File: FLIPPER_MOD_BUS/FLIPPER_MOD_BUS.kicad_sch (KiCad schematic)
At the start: 13 parts, among them J1 Conn_01x02, J2 Conn_01x10_Socket, J3 Conn_01x08_Socket, U1 SP3485EN

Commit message: UPDATE FLIPPER MODBUS SHIELD
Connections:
- net DE: now also J2.7 (Pin_7); no longer J2.6 (Pin_6)
- net RE: now also J2.8 (Pin_8); no longer J2.7 (Pin_7)
- net TX: now also J2.6 (Pin_6); no longer J2.4 (Pin_4)
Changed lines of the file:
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@@
   (no_connect (at 76.2 99.822))
   (no_connect (at 76.2 102.362))
-  (no_connect (at 45.72 110.236))
   (no_connect (at 76.2 97.282))
   (no_connect (at 76.2 109.982))
   (no_connect (at 45.72 94.996))
+  (no_connect (at 45.72 100.076))
   (wire (pts (xy 32.004 25.908) (xy 32.004 23.622))
     (stroke (width 0) (type default))
@@
     (stroke (width 0) (type default))
   )
+  (wire (pts (xy 44.196 107.696) (xy 45.72 107.696))
+    (stroke (width 0) (type default))
+  )
+  (wire (pts (xy 26.67 39.878) (xy 26.67 30.988))
+    (stroke (width 0) (type default))
+  )
+  (wire (pts (xy 26.67 23.622) (xy 26.67 25.908))
+    (stroke (width 0) (type default))
+  )
+  (wire (pts (xy 37.338 23.622) (xy 37.338 25.908))
+    (stroke (width 0) (type default))
+  )
+  (wire (pts (xy 32.004 23.622) (xy 26.67 23.622))
+    (stroke (width 0) (type default))
+  )
+  (wire (pts (xy 130.556 27.178) (xy 125.476 27.178))
+    (stroke (width 0) (type default))
+  )
+  (wire (pts (xy 36.322 117.856) (xy 36.322 115.316))
+    (stroke (width 0) (type default))
+  )
+  (wire (pts (xy 53.594 32.258) (xy 53.594 30.734))
+    (stroke (width 0) (type default))
+  )
+  (wire (pts (xy 130.556 29.464) (xy 130.556 27.178))
+    (stroke (width 0) (type default))
+  )
+  (wire (pts (xy 125.476 33.274) (xy 125.476 34.544))
+    (stroke (width 0) (type default))
+  )
+  (wire (pts (xy 89.662 30.988) (xy 89.662 28.702))
+    (stroke (width 0) (type default))
+  )
+  (wire (pts (xy 43.434 37.338) (xy 21.336 37.338))
+    (stroke (width 0) (type default))
+  )
+  (wire (pts (xy 119.634 27.178) (xy 125.476 27.178))
+    (stroke (width 0) (type default))
+  )
+  (wire (pts (xy 43.434 44.958) (xy 32.004 44.958))
+    (stroke (width 0) (type default))
+  )
+  (wire (pts (xy 36.322 97.536) (xy 36.322 99.314))
+    (stroke (width 0) (type default))
+  )
+  (wire (pts (xy 89.662 30.988) (xy 94.488 30.988))
+    (stroke (width 0) (type default))
+  )
+  (wire (pts (xy 130.556 32.004) (xy 130.556 34.544))
+    (stroke (width 0) (type default))
+  )
+  (wire (pts (xy 125.476 36.068) (xy 125.476 34.544))
+    (stroke (width 0) (type default))
+  )
+  (wire (pts (xy 44.196 110.236) (xy 45.72 110.236))
+    (stroke (width 0) (type default))
+  )
+  (wire (pts (xy 21.336 23.622) (xy 26.67 23.622))
+    (stroke (width 0) (type default))
+  )
+  (wire (pts (xy 45.72 97.536) (xy 36.322 97.536))
+    (stroke (width 0) (type default))
+  )
+  (wire (pts (xy 130.556 34.544) (xy 125.476 34.544))
+    (stroke (width 0) (type default))
+  )
+  (wire (pts (xy 83.82 40.894) (xy 89.916 40.894))
+    (stroke (width 0) (type default))
+  )
+  (wire (pts (xy 45.72 92.456) (xy 38.862 92.456))
+    (stroke (width 0) (type default))
+  )
   (wire (pts (xy 44.196 105.156) (xy 45.72 105.156))
     (stroke (width 0) (type default))
   )
-  (wire (pts (xy 26.67 39.878) (xy 26.67 30.988))
-    (stroke (width 0) (type default))
-  )
-  (wire (pts (xy 26.67 23.622) (xy 26.67 25.908))
-    (stroke (width 0) (type default))
-  )
-  (wire (pts (xy 37.338 23.622) (xy 37.338 25.908))
-    (stroke (width 0) (type default))
-  )
-  (wire (pts (xy 32.004 23.622) (xy 26.67 23.622))
-    (stroke (width 0) (type default))
-  )
-  (wire (pts (xy 130.556 27.178) (xy 125.476 27.178))
-    (stroke (width 0) (type default))
-  )
-  (wire (pts (xy 36.322 117.856) (xy 36.322 115.316))
-    (stroke (width 0) (type default))
-  )
-  (wire (pts (xy 53.594 32.258) (xy 53.594 30.734))
-    (stroke (width 0) (type default))
-  )
-  (wire (pts (xy 130.556 29.464) (xy 130.556 27.178))
-    (stroke (width 0) (type default))
-  )
-  (wire (pts (xy 125.476 33.274) (xy 125.476 34.544))
-    (stroke (width 0) (type default))
-  )
-  (wire (pts (xy 89.662 30.988) (xy 89.662 28.702))
-    (stroke (width 0) (type default))
-  )
-  (wire (pts (xy 43.434 37.338) (xy 21.336 37.338))
-    (stroke (width 0) (type default))
-  )
-  (wire (pts (xy 119.634 27.178) (xy 125.476 27.178))
-    (stroke (width 0) (type default))
-  )
-  (wire (pts (xy 43.434 44.958) (xy 32.004 44.958))
-    (stroke (width 0) (type default))
-  )
-  (wire (pts (xy 36.322 97.536) (xy 36.322 99.314))
-    (stroke (width 0) (type default))
-  )
-  (wire (pts (xy 89.662 30.988) (xy 94.488 30.988))
-    (stroke (width 0) (type default))
-  )
-  (wire (pts (xy 130.556 32.004) (xy 130.556 34.544))
-    (stroke (width 0) (type default))
-  )
-  (wire (pts (xy 125.476 36.068) (xy 125.476 34.544))
-    (stroke (width 0) (type default))
-  )
-  (wire (pts (xy 44.196 107.696) (xy 45.72 107.696))
-    (stroke (width 0) (type default))
-  )
-  (wire (pts (xy 21.336 23.622) (xy 26.67 23.622))
-    (stroke (width 0) (type default))
-  )
-  (wire (pts (xy 45.72 97.536) (xy 36.322 97.536))
-    (stroke (width 0) (type default))
-  )
-  (wire (pts (xy 130.556 34.544) (xy 125.476 34.544))
-    (stroke (width 0) (type default))
-  )
-  (wire (pts (xy 83.82 40.894) (xy 89.916 40.894))
-    (stroke (width 0) (type default))
-  )
-  (wire (pts (xy 45.72 92.456) (xy 38.862 92.456))
+  (wire (pts (xy 37.338 20.32) (xy 37.338 23.622))
+    (stroke (width 0) (type default))
+  )
+  (wire (pts (xy 36.322 115.316) (xy 45.72 115.316))
+    (stroke (width 0) (type default))
+  )
+  (wire (pts (xy 43.434 39.878) (xy 26.67 39.878))
+    (stroke (width 0) (type default))
+  )
+  (wire (pts (xy 38.862 92.456) (xy 38.862 91.694))
+    (stroke (width 0) (type default))
+  )
+  (wire (pts (xy 16.256 39.878) (xy 26.67 39.878))
+    (stroke (width 0) (type default))
+  )
+  (wire (pts (xy 125.476 27.178) (xy 125.476 28.194))
+    (stroke (width 0) (type default))
+  )
+  (wire (pts (xy 83.82 30.988) (xy 89.662 30.988))
+    (stroke (width 0) (type default))
+  )
+  (wire (pts (xy 37.338 47.498) (xy 37.338 30.988))
+    (stroke (width 0) (type default))
+  )
+  (wire (pts (xy 16.002 47.498) (xy 37.338 47.498))
+    (stroke (width 0) (type default))
+  )
+  (wire (pts (xy 125.476 21.336) (xy 125.476 19.558))
+    (stroke (width 0) (type default))
+  )
+  (wire (pts (xy 21.336 25.908) (xy 21.336 23.622))
     (stroke (width 0) (type default))
   )
   (wire (pts (xy 44.196 102.616) (xy 45.72 102.616))
-    (stroke (width 0) (type default))
-  )
-  (wire (pts (xy 37.338 20.32) (xy 37.338 23.622))
-    (stroke (width 0) (type default))
-  )
-  (wire (pts (xy 36.322 115.316) (xy 45.72 115.316))
-    (stroke (width 0) (type default))
-  )
-  (wire (pts (xy 43.434 39.878) (xy 26.67 39.878))
-    (stroke (width 0) (type default))
-  )
-  (wire (pts (xy 38.862 92.456) (xy 38.862 91.694))
-    (stroke (width 0) (type default))
-  )
-  (wire (pts (xy 16.256 39.878) (xy 26.67 39.878))
-    (stroke (width 0) (type default))
-  )
-  (wire (pts (xy 125.476 27.178) (xy 125.476 28.194))
-    (stroke (width 0) (type default))
-  )
-  (wire (pts (xy 83.82 30.988) (xy 89.662 30.988))
-    (stroke (width 0) (type default))
-  )
-  (wire (pts (xy 37.338 47.498) (xy 37.338 30.988))
-    (stroke (width 0) (type default))
-  )
-  (wire (pts (xy 16.002 47.498) (xy 37.338 47.498))
-    (stroke (width 0) (type default))
-  )
-  (wire (pts (xy 125.476 21.336) (xy 125.476 19.558))
-    (stroke (width 0) (type default))
-  )
-  (wire (pts (xy 21.336 25.908) (xy 21.336 23.622))
-    (stroke (width 0) (type default))
-  )
-  (wire (pts (xy 44.196 100.076) (xy 45.72 100.076))
     (stroke (width 0) (type default))
   )
@@
     (effects (font (size 1.27 1.27)) (justify right bottom))
   )
-  (label "DE" (at 44.196 105.156 180) (fields_autoplaced)
+  (label "DE" (at 44.196 107.696 180) (fields_autoplaced)
     (effects (font (size 1.27 1.27)) (justify right bottom))
   )
@@
     (effects (font (size 1.27 1.27)) (justify right bottom))
   )
-  (label "TX" (at 44.196 100.076 180) (fields_autoplaced)
+  (label "TX" (at 44.196 105.156 180) (fields_autoplaced)
     (effects (font (size 1.27 1.27)) (justify right bottom))
   )
@@
     (effects (font (size 1.27 1.27)) (justify right bottom))
   )
-  (label "RE" (at 44.196 107.696 180) (fields_autoplaced)
-    (effects (font (size 1.27 1.27)) (justify right bottom))
-  )
+  (label "RE" (at 44.196 110.236 180) (fields_autoplaced)
+    (effects (font (size 1.27 1.27)) (justify right bottom))
+  )

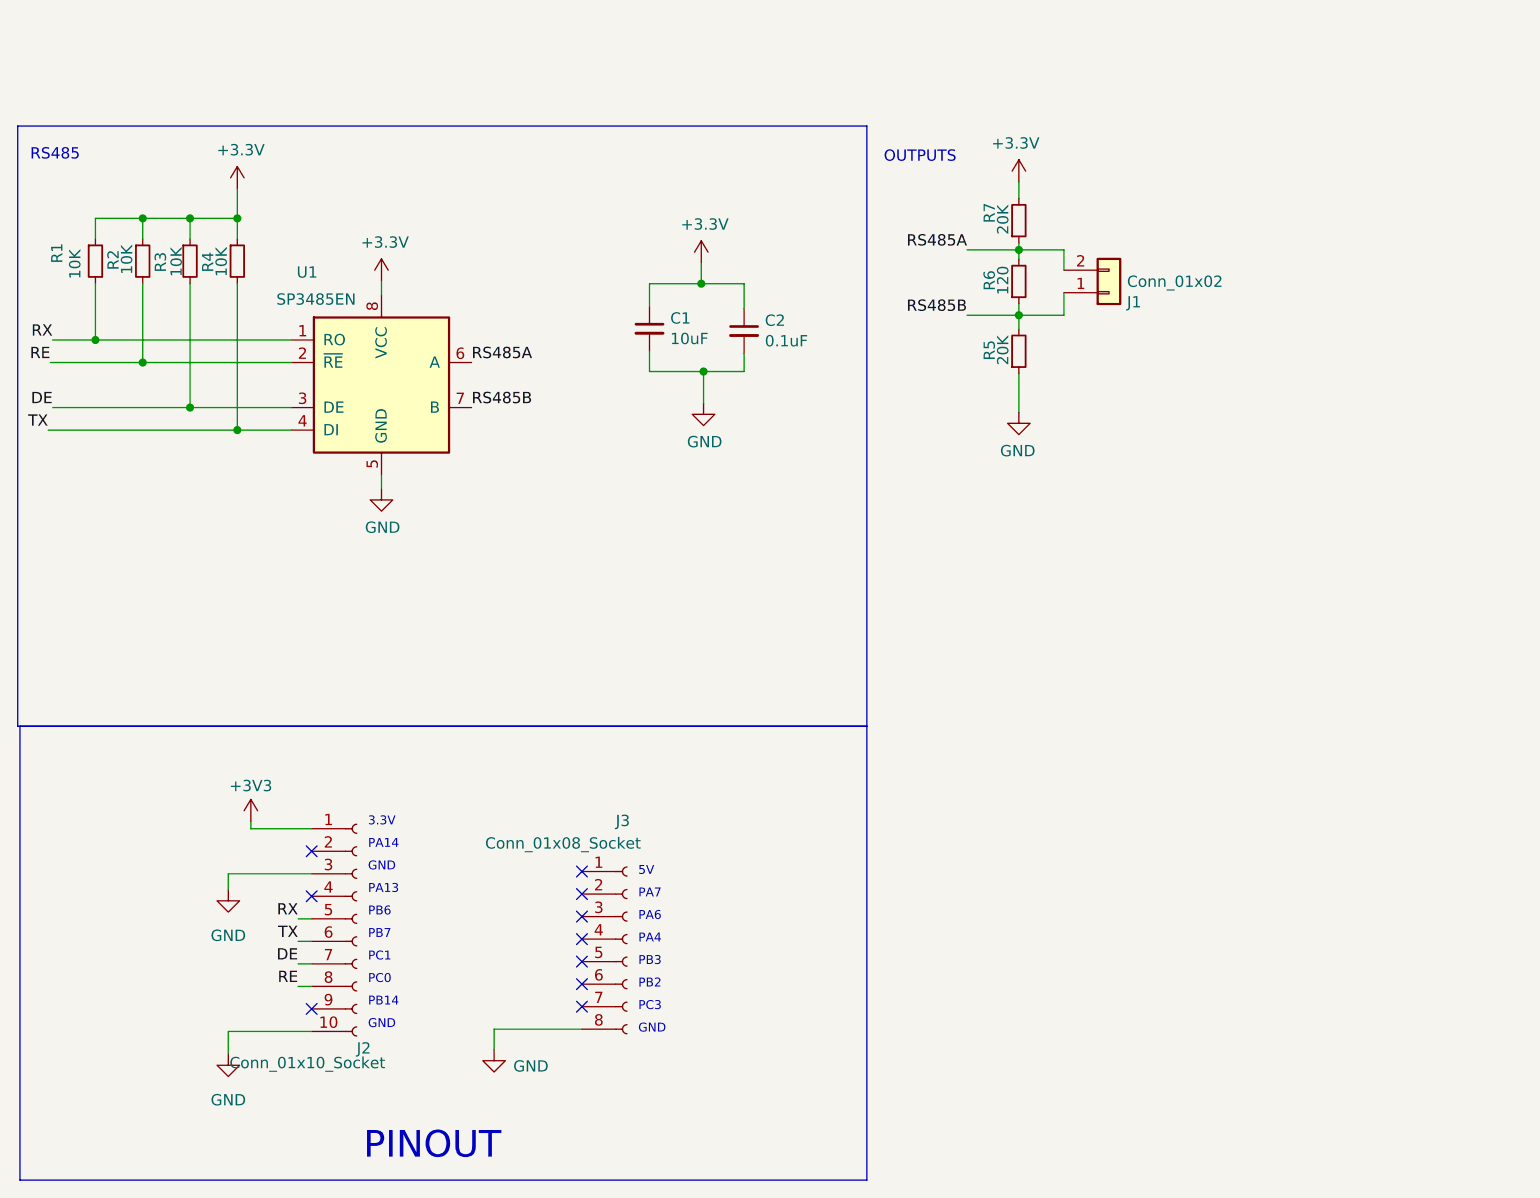
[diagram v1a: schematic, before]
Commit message: Flipper_MOD_BUS RX TX Fixed
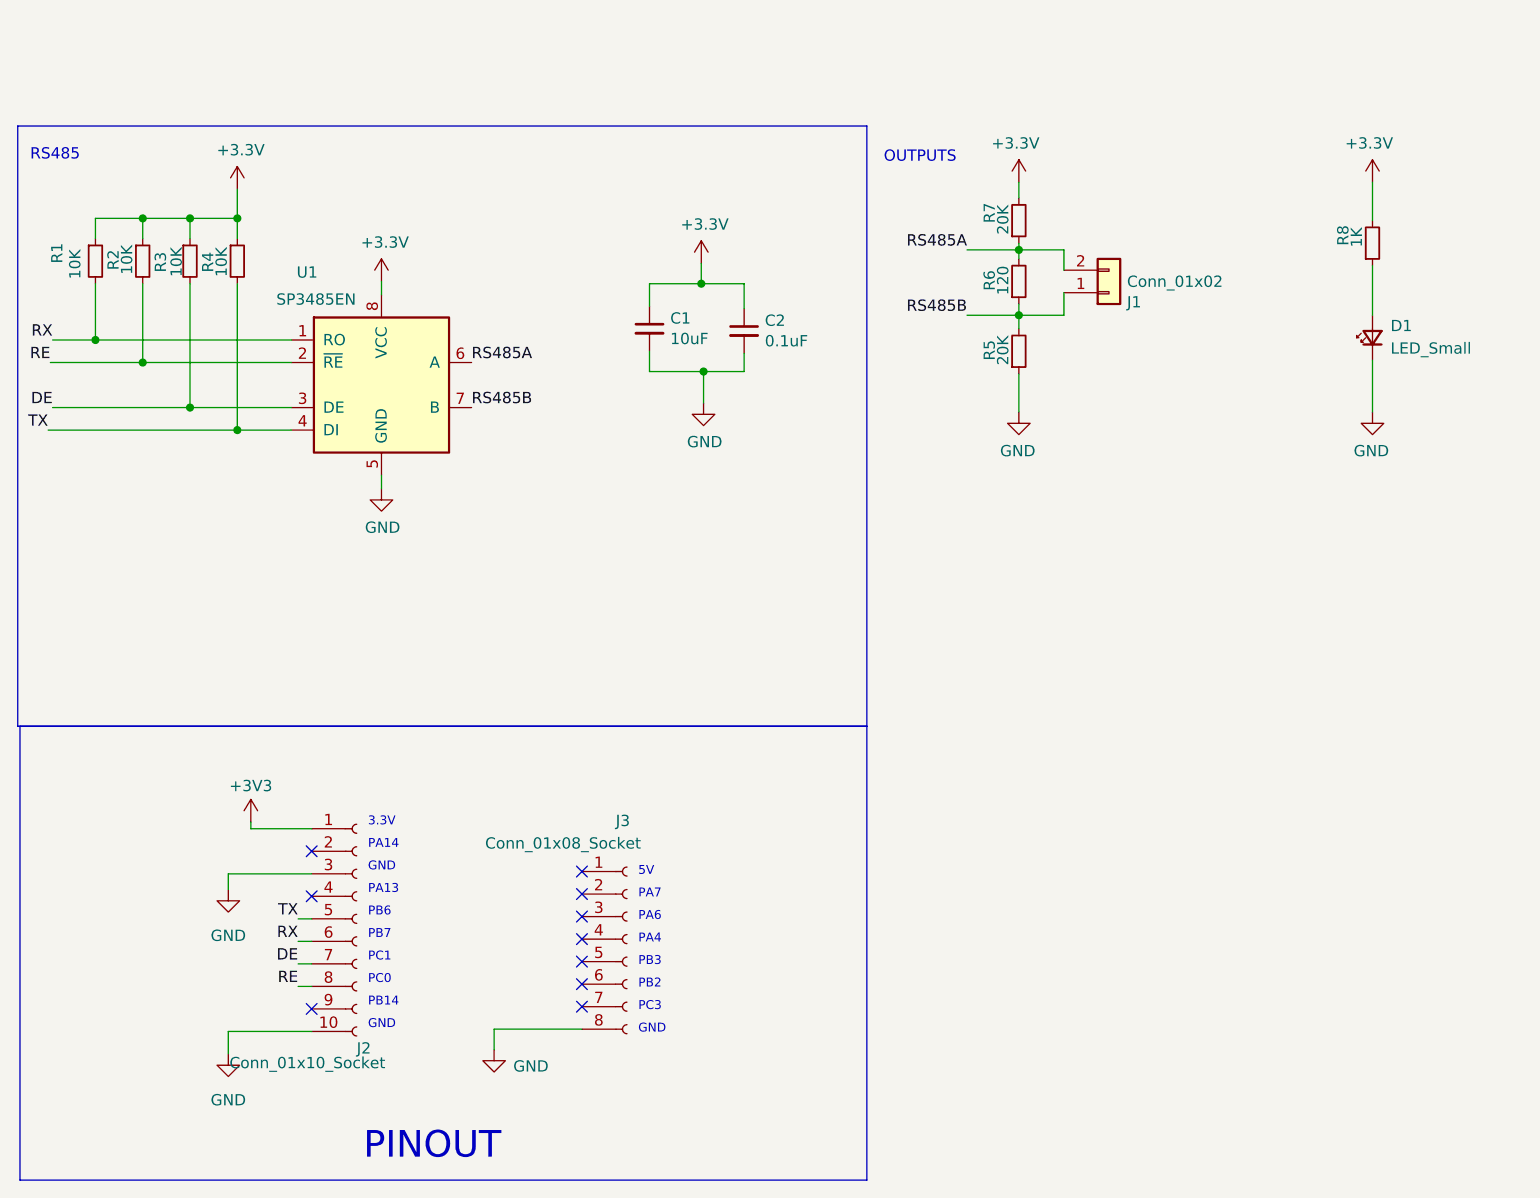
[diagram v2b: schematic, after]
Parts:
- added D1: LED_Small, LED_SMD:LED_0603_1608Metric_Pad1.05x0.95mm_HandSolder, symbol Device:LED_Small
- added R8: 1K, Resistor_SMD:R_0603_1608Metric_Pad0.98x0.95mm_HandSolder, symbol Device:R_Small
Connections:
- net +3V3: now also R8.2
- net GND: now also D1.1 (K)
- net RX: now also J2.6 (Pin_6); no longer J2.5 (Pin_5)
- net TX: now also J2.5 (Pin_5); no longer J2.6 (Pin_6)
- new net: D1.2 (A), R8.1
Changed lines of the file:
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@@
   (no_connect (at 45.72 94.996))
   (no_connect (at 45.72 100.076))
+  (wire (pts (xy 165.354 39.624) (xy 165.354 45.466))
+    (stroke (width 0) (type default))
+  )
   (wire (pts (xy 32.004 25.908) (xy 32.004 23.622))
     (stroke (width 0) (type default))
@@
     (stroke (width 0) (type default))
   )
+  (wire (pts (xy 165.354 19.558) (xy 165.354 23.876))
+    (stroke (width 0) (type default))
+  )
   (wire (pts (xy 130.556 27.178) (xy 125.476 27.178))
     (stroke (width 0) (type default))
@@
   )
   (wire (pts (xy 21.336 23.622) (xy 26.67 23.622))
+    (stroke (width 0) (type default))
+  )
+  (wire (pts (xy 165.354 28.956) (xy 165.354 34.544))
     (stroke (width 0) (type default))
   )
@@
     (effects (font (size 1.27 1.27)) (justify left bottom))
   )
-  (label "RX" (at 44.196 102.616 180) (fields_autoplaced)
+  (label "RX" (at 44.196 105.156 180) (fields_autoplaced)
     (effects (font (size 1.27 1.27)) (justify right bottom))
   )
@@
     (effects (font (size 1.27 1.27)) (justify right bottom))
   )
-  (label "TX" (at 44.196 105.156 180) (fields_autoplaced)
+  (label "TX" (at 44.196 102.616 180) (fields_autoplaced)
     (effects (font (size 1.27 1.27)) (justify right bottom))
   )
@@
         (path "/000d5789-2d2c-436e-a8f3-713f1968a92a"
           (reference "C1") (unit 1)
+        )
+      )
+    )
+  )
+  (symbol (lib_id "power:GND") (at 165.354 45.466 0) (mirror y) (unit 1)
+    (in_bom yes) (on_board yes) (dnp no)
+    (property "Reference" "#PWR09" (at 165.354 51.816 0)
+      (effects (font (size 1.27 1.27)) hide)
+    )
+    (property "Value" "GND" (at 165.227 49.8602 0)
+      (effects (font (size 1.27 1.27)))
+    )
+    (property "Footprint" "" (at 165.354 45.466 0)
+      (effects (font (size 1.27 1.27)) hide)
+    )
+    (property "Datasheet" "" (at 165.354 45.466 0)
+      (effects (font (size 1.27 1.27)) hide)
+    )
+    (pin "1")
+    (instances
+      (project "FLIPPER_MOD_BUS"
+        (path "/000d5789-2d2c-436e-a8f3-713f1968a92a"
+          (reference "#PWR09") (unit 1)
+        )
+      )
+    )
+  )
+  (symbol (lib_id "Device:LED_Small") (at 165.354 37.084 90) (unit 1)
+    (in_bom yes) (on_board yes) (dnp no) (fields_autoplaced)
+    (property "Reference" "D1" (at 167.386 35.7505 90)
+      (effects (font (size 1.27 1.27)) (justify right))
+    )
+    (property "Value" "LED_Small" (at 167.386 38.2905 90)
+      (effects (font (size 1.27 1.27)) (justify right))
+    )
+    (property "Footprint" "LED_SMD:LED_0603_1608Metric_Pad1.05x0.95mm_HandSolder" (at 165.354 37.084 90)
+      (effects (font (size 1.27 1.27)) hide)
+    )
+    (property "Datasheet" "~" (at 165.354 37.084 90)
+      (effects (font (size 1.27 1.27)) hide)
+    )
+    (pin "2")
+    (pin "1")
+    (instances
+      (project "FLIPPER_MOD_BUS"
+        (path "/000d5789-2d2c-436e-a8f3-713f1968a92a"
+          (reference "D1") (unit 1)
         )
       )
@@
     )
   )
+  (symbol (lib_id "power:+3.3V") (at 165.354 19.558 0) (mirror y) (unit 1)
+    (in_bom yes) (on_board yes) (dnp no)
+    (property "Reference" "#PWR08" (at 165.354 23.368 0)
+      (effects (font (size 1.27 1.27)) hide)
+    )
+    (property "Value" "+3.3V" (at 164.973 15.1638 0)
+      (effects (font (size 1.27 1.27)))
+    )
+    (property "Footprint" "" (at 165.354 19.558 0)
+      (effects (font (size 1.27 1.27)) hide)
+    )
+    (property "Datasheet" "" (at 165.354 19.558 0)
+      (effects (font (size 1.27 1.27)) hide)
+    )
+    (pin "1")
+    (instances
+      (project "FLIPPER_MOD_BUS"
+        (path "/000d5789-2d2c-436e-a8f3-713f1968a92a"
+          (reference "#PWR08") (unit 1)
+        )
+      )
+    )
+  )
   (symbol (lib_id "power:GND") (at 125.476 45.466 0) (mirror y) (unit 1)
     (in_bom yes) (on_board yes) (dnp no)
@@
         )
       )
+    )
+  )
+  (symbol (lib_id "Device:R_Small") (at 165.354 26.416 0) (mirror x) (unit 1)
+    (in_bom yes) (on_board yes) (dnp no)
+    (property "Reference" "R8" (at 162.052 24.384 90)
+      (effects (font (size 1.27 1.27)) (justify left))
+    )
+    (property "Value" "1K" (at 163.576 24.638 90)
+      (effects (font (size 1.27 1.27)) (justify left))
+    )
+    (property "Footprint" "Resistor_SMD:R_0603_1608Metric_Pad0.98x0.95mm_HandSolder" (at 165.354 26.416 0)
+      (effects (font (size 1.27 1.27)) hide)
+    )
+    (property "Datasheet" "https://lcsc.com/product-detail/Chip-Resistor-Surface-Mount_UNI-ROYAL-Uniroyal-Elec-0603WAJ0203T5E_C25586.html" (at 165.354 26.416 0)
+      (effects (font (size 1.27 1.27)) hide)
+    )
+    (property "manf#" "0603WAJ0203T5E" (at 165.354 26.416 0)
+      (effects (font (size 1.27 1.27)) hide)
+    )
+    (property "LCSC#" "C25586" (at 165.354 26.416 0)
+      (effects (font (size 1.27 1.27)) hide)
+    )
+    (property "Proveedor" "LCSC" (at 165.354 26.416 0)
+      (effects (font (size 1.27 1.27)) hide)
+    )
+    (pin "1")
+    (pin "2")
+    (instances
+      (project "FLIPPER_MOD_BUS"
+        (path "/000d5789-2d2c-436e-a8f3-713f1968a92a"
+          (reference "R8") (unit 1)
+        )
+      )
